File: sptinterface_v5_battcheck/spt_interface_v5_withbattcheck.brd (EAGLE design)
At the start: 88.6 x 39.4 mm, 32 parts, among them X1 2516-

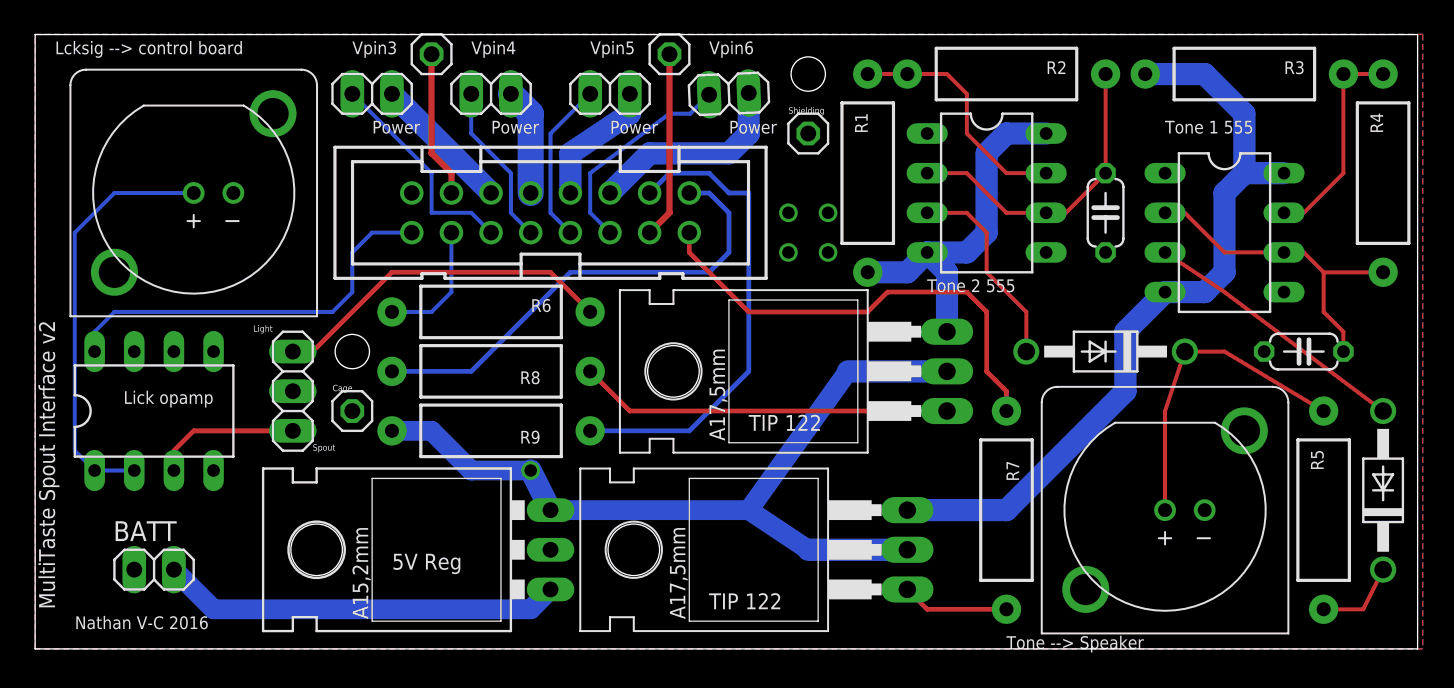
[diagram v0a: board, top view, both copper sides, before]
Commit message: Update PCBs, add IR option
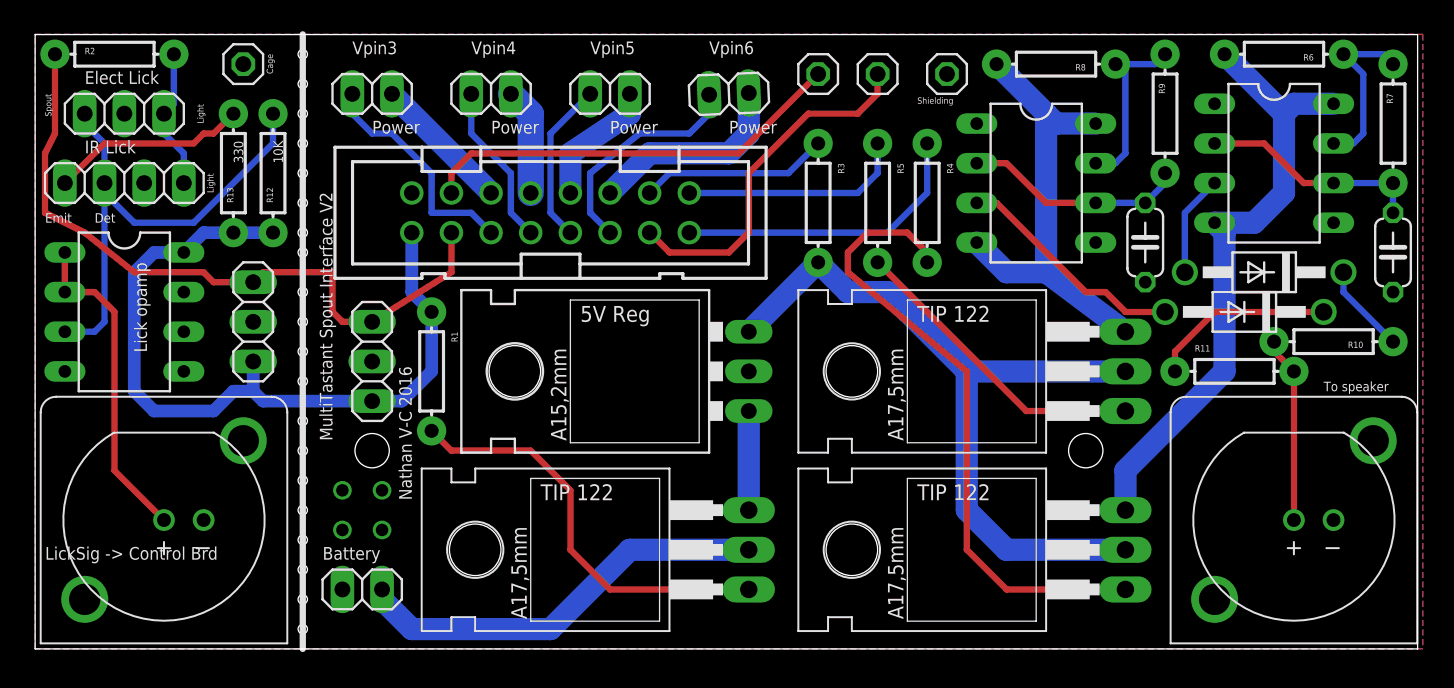
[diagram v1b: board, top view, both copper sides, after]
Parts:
- removed FLR: (no value), pinhead:1X01
- added FLR2: (no value), pinhead:1X01
- added JP3, JP5: (no value), pinhead:1X03
- added JP6: (no value), pinhead:1X04
- added R10, R11, R12, R13: (no value), SparkFun-Resistors:AXIAL-0.3EZ
- added VRSWITCH: TIP122, transistor-npn:TO220
- R1, R2, R3, R4, R5, R6, R7, R8, R9: device SparkFun-Resistors:AXIAL-0.5 -> SparkFun-Resistors:AXIAL-0.3EZ
- moved R2 57.2 mm to (5.08, 38.1), turned to 0 degrees
- moved R6 53.4 mm to (80.0, 38.1), turned to 180 degrees
- moved R9 47.7 mm to (72.4, 34.3), turned to 90 degrees
- moved R8 41.2 mm to (65.4, 37.5)
- moved R7 35.0 mm to (87.0, 33.7), turned to 90 degrees
- moved R5 34.7 mm to (54.0, 28.6), turned to 270 degrees
- moved R1 30.7 mm to (25.4, 17.8)
- moved R4 29.3 mm to (57.1, 28.6), turned to 270 degrees
- moved R3 28.5 mm to (50.2, 28.6), turned to 270 degrees
- moved JP1 24.8 mm to (50.2, 36.8)
- moved LCKSIG 21.0 mm to (8.26, 8.26)
- moved VREG_5V 17.1 mm to (41.9, 17.8)
- moved D2 15.9 mm to (78.7, 24.1), turned to 180 degrees
- moved TN2TR 14.0 mm to (63.5, 6.35)
- moved JP2 13.4 mm to (54.0, 36.8)
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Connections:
- new net N$29: VREG_5V.IN, VRSWITCH.3
- new net N$32: R1.P$2, VRSWITCH.1
- new net N$33: D1.C, R11.P$1
- new net N$36: JP6.4, R13.P$2
- net GND: now also FLR2.1, JP3.2, JP5.2, JP6.2; no longer FLR.1
- net N$1: now also R3.P$1; no longer R9.P$1
- net N$11: now also R6.P$1, R7.P$2; no longer R3.P$1, R4.P$2
- net N$12: now also R8.P$1, R9.P$2; no longer R1.P$1, R2.P$2
- net N$13: now also R7.P$1; no longer R4.P$1
- net N$14: now also R9.P$1; no longer R2.P$1
- net N$17: now also R10.P$2, R11.P$2; no longer D1.C, R5.P$2
- net N$18: now also JP3.1, R2.P$1, X1.3; no longer R6.P$2
- net N$19: now also JP5.1, JP6.1, R2.P$2; no longer R6.P$1, X1.3
- net N$2: now also VRSWITCH.2; no longer VREG_5V.IN
- net N$27: now also R6.P$2; no longer R3.P$2
- net N$28: now also JP5.3, JP6.3, R12.P$2; no longer JP4.3
- net N$3: now also R4.P$2; no longer R7.P$2
- net N$34: now also R5.P$1; no longer R8.P$2
- net N$35: now also R3.P$2; no longer R9.P$2
- net N$4: now also R5.P$2; no longer R8.P$1
- net N$5: now also R8.P$2; no longer R1.P$2
- net N$6: now also R10.P$1; no longer R5.P$1
- net N$7: now also R4.P$1; no longer R7.P$1
- net N$8: now also JP3.3, JP4.3, R1.P$1, R12.P$1, R13.P$1
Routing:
- net N$3: track 6.88 -> 40.6 mm
- net N$32: track 0.00 -> 26.8 mm
- net N$8: track 25.7 -> 50.0 mm
- net N$28: track 9.42 -> 32.3 mm
- net N$18: track 22.2 -> 44.3 mm
- net N$1: track 30.6 -> 12.1 mm
- net N$30: track 9.42 -> 27.4 mm
- net N$34: track 30.4 -> 14.5 mm
- net N$36: track 0.00 -> 12.6 mm
- net N$33: track 0.00 -> 11.8 mm
- net N$31: track 12.0 -> 22.8 mm
- net N$15: track 17.3 -> 6.50 mm
- net N$7: track 29.8 -> 19.5 mm
- net N$27: track 49.5 -> 40.4 mm
- net N$17: track 20.3 -> 12.0 mm
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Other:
- board text added: "10K"
- board text added: "330"
- board text added: "Battery"
- board text added: "Det"
- board text added: "Elect Lick"
- board text added: "Emit"
- board text added: "IR Lick"
- board text added: "LickSig -> Control Brd"
- board text added: "MultiTastant Spout Interface V2"
- board text added: "To speaker"
- board text removed: "Lcksig --> control board"
- board text removed: "MultiTaste Spout Interface v2"
- board text removed: "R1"
- board text removed: "R2"
- board text removed: "R3"
- board text removed: "R4"
- board text removed: "R5"
- board text removed: "R6"
- board text removed: "Tone --> Speaker"
- board text removed: "Tone 1 555"
- board text removed: "Tone 2 555"
